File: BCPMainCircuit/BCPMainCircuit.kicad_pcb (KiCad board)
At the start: 2 copper layers, 8 parts, among them SW1 SW_Nidec_CAS-120A1, U1 LD1117V33, U2 Pico 2, U3 DEV-13712, U6 BME280

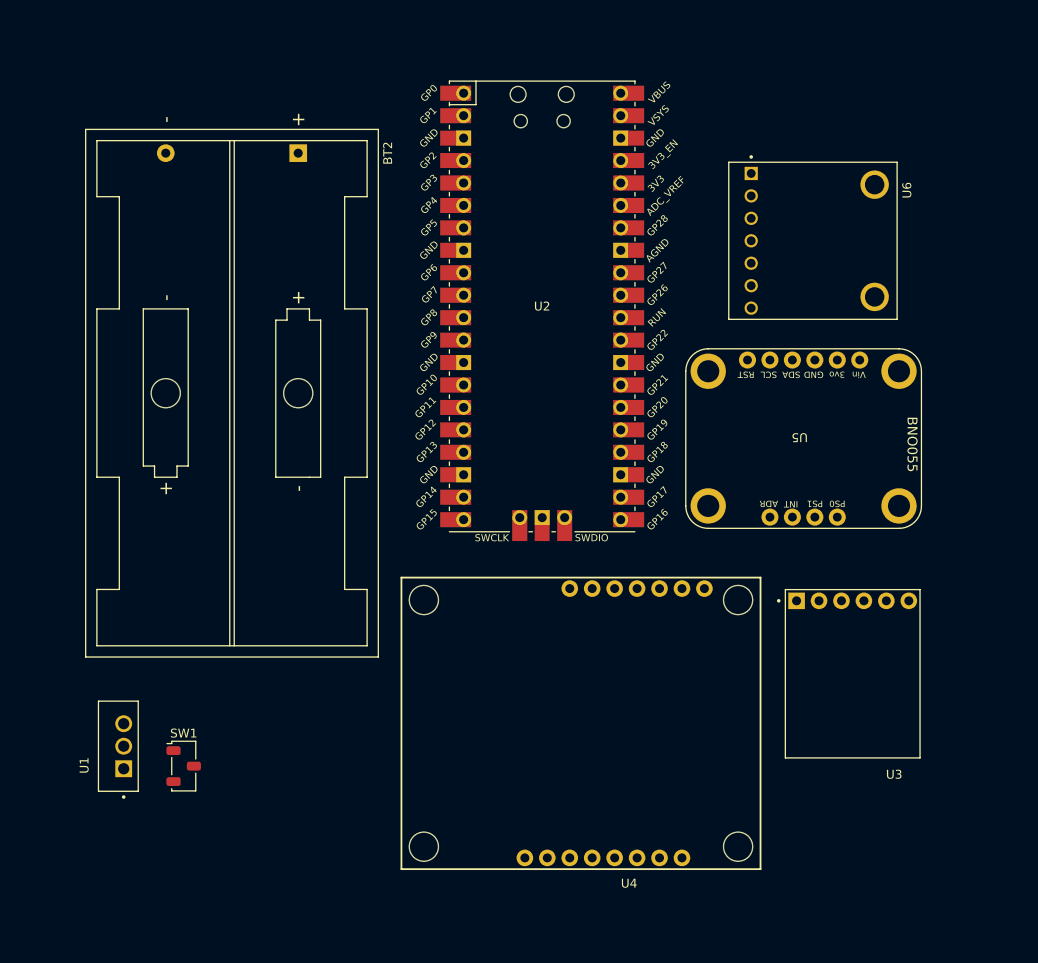
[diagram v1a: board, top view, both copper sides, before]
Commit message: Added silkscreen updates
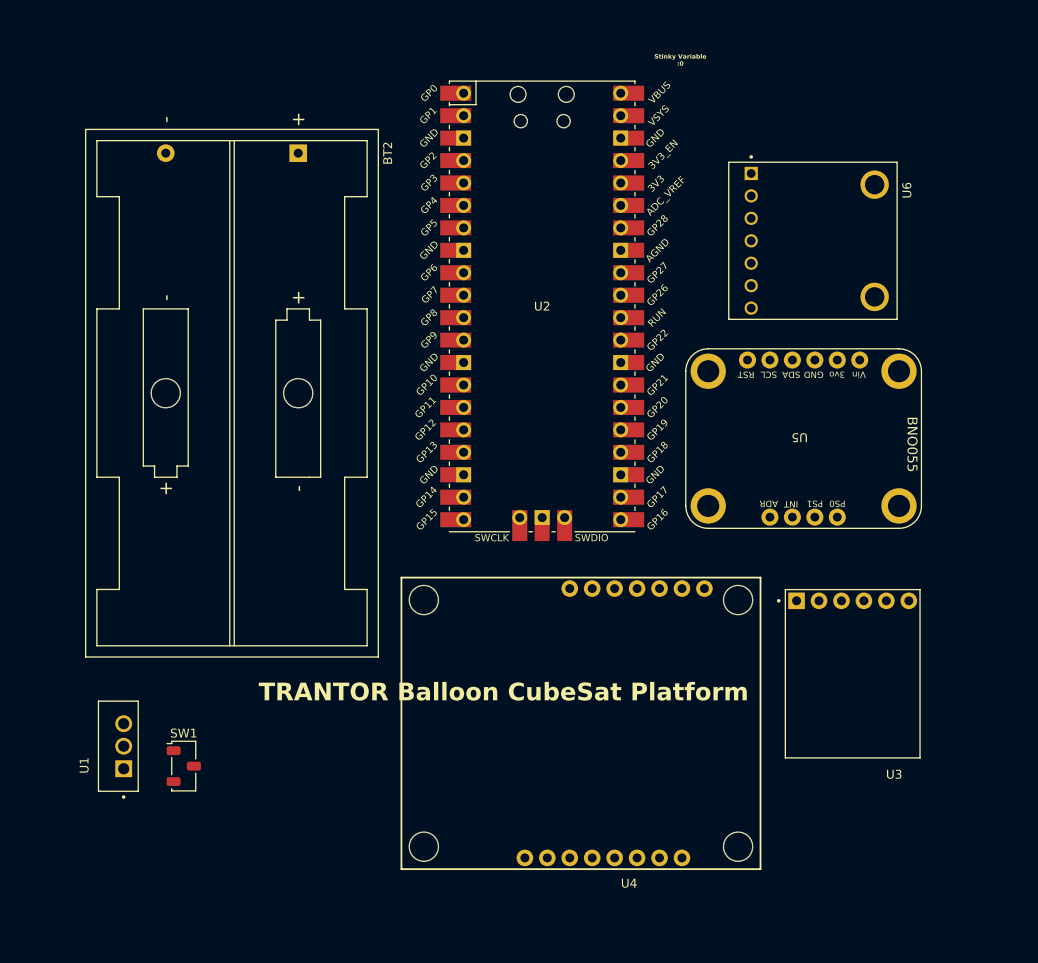
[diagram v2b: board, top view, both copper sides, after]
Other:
- board text added: "Stinky Variable :0"
- board text added: "TRANTOR Balloon CubeSat Platform"
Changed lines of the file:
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@@
 		(layer "Eco2.User")
+	)
+	(gr_text "TRANTOR Balloon CubeSat Platform"
+		(at 122 101 0)
+		(layer "F.SilkS")
+		(effects
+			(font
+				(size 2 2)
+				(thickness 0.4)
+				(bold yes)
+			)
+			(justify bottom)
+		)
+	)
+	(gr_text "Stinky Variable\n:0"
+		(at 142 29 0)
+		(layer "F.SilkS")
+		(effects
+			(font
+				(size 0.5 0.5)
+				(thickness 0.125)
+				(bold yes)
+			)
+			(justify bottom)
+		)
 	)
 	(segment

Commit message: Update cutout
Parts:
- BT2, U4, U6: moved to B.Cu
- moved BT2 60.5 mm to (102.2, 99.3), turned to 90 degrees
- moved U5 39.9 mm to (124.7, 95.8), turned to 0 degrees
- moved U6 38.9 mm to (155.2, 87.6), turned to 180 degrees
- moved U4 28.0 mm to (114.4, 111.6), turned to 180 degrees
- moved U1 20.7 mm to (98.8, 109.1), turned to -90 degrees
- moved U2 11.9 mm to (137.8, 59.5), turned to 90 degrees
- moved U3 6.45 mm to (155.1, 97.6)
- moved SW1 5.77 mm to (91.4, 106.9), turned to 180 degrees
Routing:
- net (no net): vias 0 -> 4
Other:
- board outline added: 94 x 88 mm
- board text removed: "Stinky Variable :0"

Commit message: Silkscreen Fixes
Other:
- board text added: "Stinky Variable :0"
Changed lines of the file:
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@@
 		(layer "Edge.Cuts")
 	)
+	(gr_text "Stinky Variable\n:0"
+		(at 154 114 0)
+		(layer "F.SilkS")
+		(effects
+			(font
+				(size 1 1)
+				(thickness 0.1)
+			)
+			(justify bottom)
+		)
+	)
 	(gr_text "TRANTOR Balloon CubeSat Platform"
-		(at 112.705 104.37 -90)
-		(layer "B.SilkS")
+		(at 119.5 40 0)
+		(layer "F.SilkS")
 		(effects
 			(font
@@
 				(bold yes)
 			)
-			(justify bottom mirror)
+			(justify bottom)
 		)
 	)

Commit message: Traces Run for V1
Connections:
- BT2 pad 2: Net-(BT1-+) -> GND
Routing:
- net /3.3 V: track 0.00 -> 99.6 mm
- net /SCL: track 0.00 -> 83.9 mm, vias 0 -> 2
- net /SDA: track 0.00 -> 82.6 mm, vias 0 -> 1
- net /MCUTX: track 0.00 -> 56.7 mm
- net /MCURX: track 0.00 -> 54.7 mm, vias 0 -> 1
- net GND: track 0.00 -> 29.1 mm
- net Net-(BT2-+): track 0.00 -> 15.7 mm
- net Net-(SW1-A): track 0.00 -> 8.89 mm
- added copper zone on B.Cu, net GND

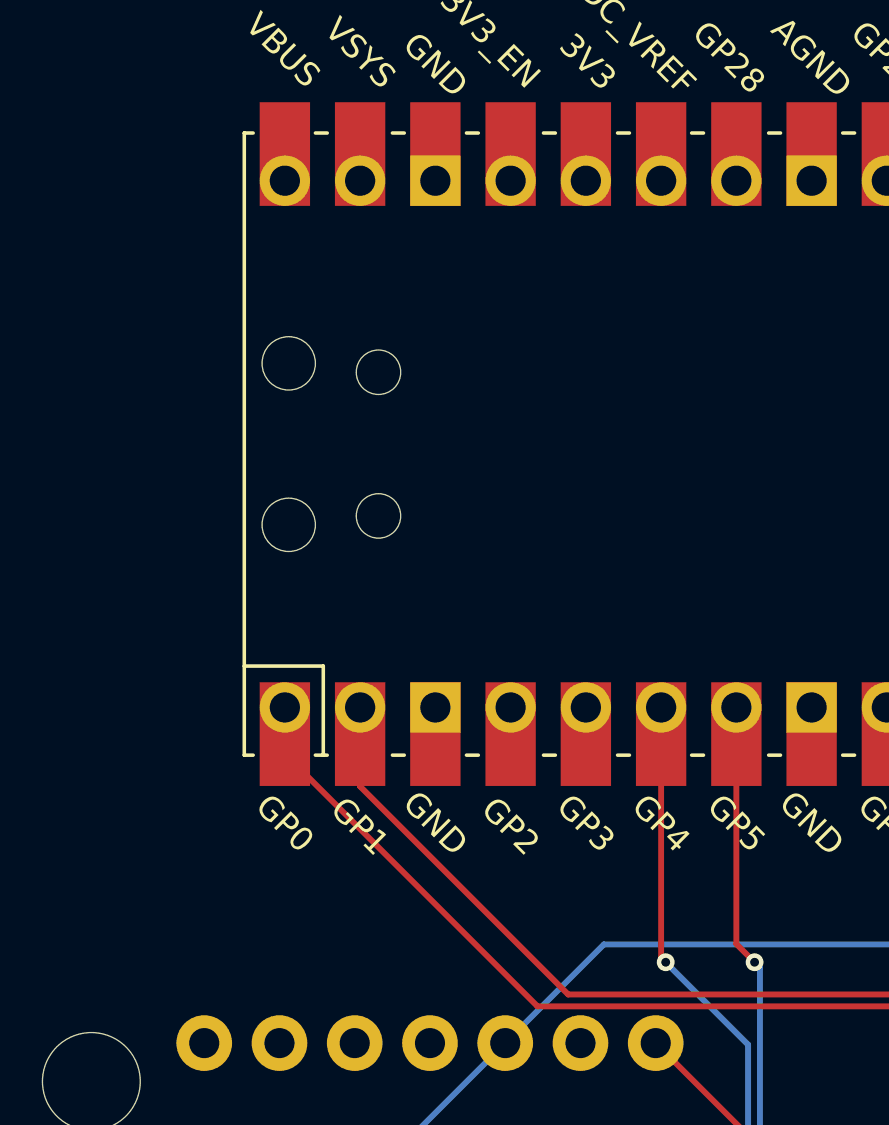
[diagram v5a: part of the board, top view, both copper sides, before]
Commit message: Powering the pico, whoops
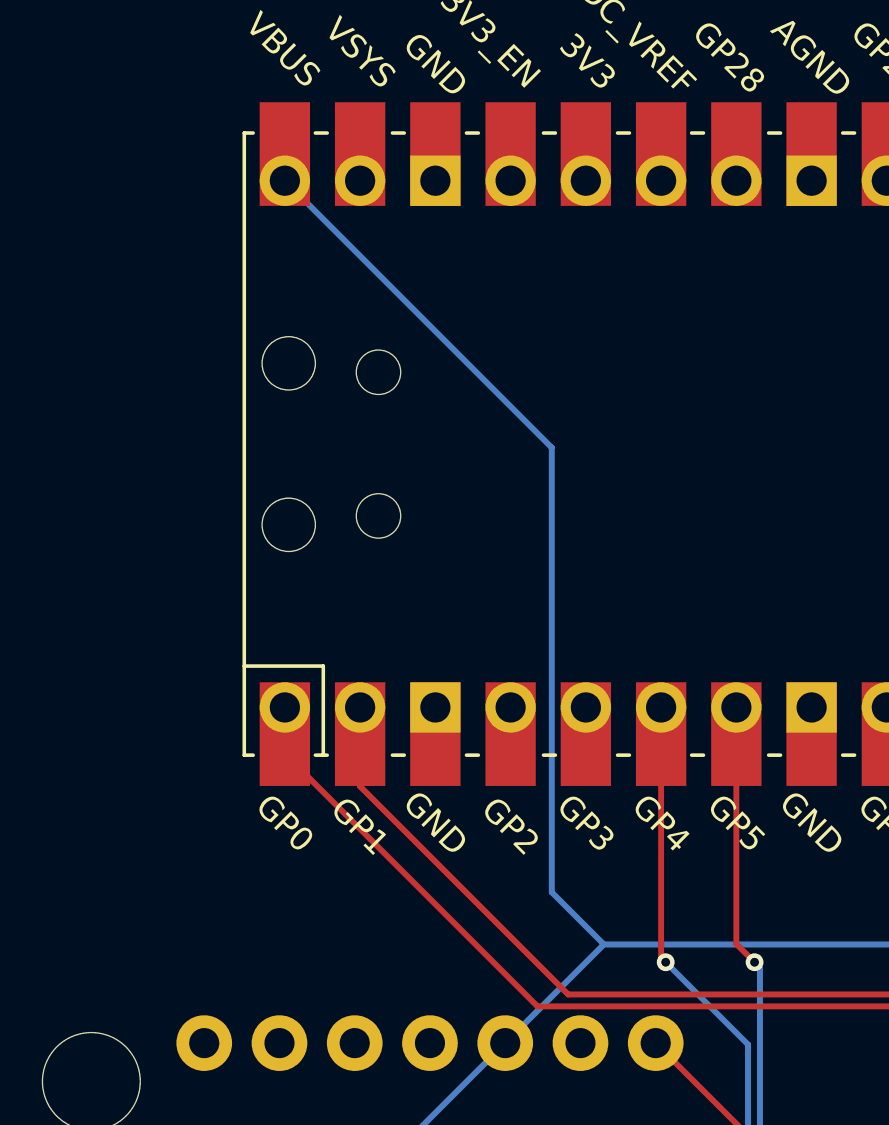
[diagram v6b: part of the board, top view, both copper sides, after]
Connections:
- U2 pad 40: unconnected-(U2-VBUS-Pad40) -> /3.3 V
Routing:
- net /3.3 V: track 99.6 -> 129.8 mm
